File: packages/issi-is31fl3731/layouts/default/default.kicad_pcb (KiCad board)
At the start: 2 copper layers, 11 parts

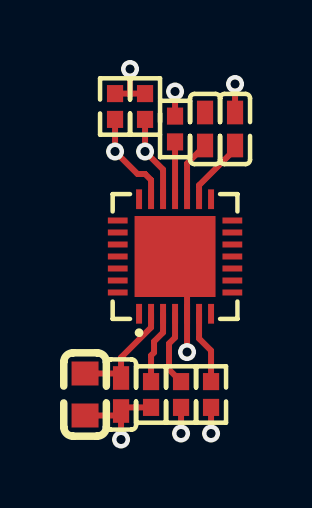
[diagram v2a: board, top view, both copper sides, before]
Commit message: Upgrade Packages: Narayans Half (#185)
* adi-ad5693r

* fix frozen

* prjc-teensy_4_1

* rp2040

* adi-adxl375: Add missing usage build target to ato.yaml

* adi-ds2482s-800: Update layout files after build

* adi-ltc4311: Update layout to fix frozen build

- Updated net names (BUS1/BUS2 → SDA/SCL, gnd → GND, hv → VCC)
- Fixed footprint properties and coordinates
- Package now passes frozen build and verification

* awinic-aw9523: Update layout to fix frozen build

- Updated net names (AD0/AD1 → address_bit_0/address_bit_1, hv → VCC, gnd → GND)
- Updated GPIO line names (-line-0 → gpios[8]-line, etc.)
- Fixed footprint properties and coordinates
- Package now passes frozen build and verification

* awinic-aw9523: Bump version to 0.1.1

- Version bump due to layout updates to fix frozen build

* adi-adbms6830: Fix package verify issues

- Add has_part_removed trait to components missing pickers (atopile_logo, SPDT, analog_DPDT)
- Add missing import for has_part_removed trait
- Add exclude_checks to usage build in ato.yaml
- Update README.md to match usage.ato content
- Bump version from 0.1.2 to 0.1.3

Package now passes ato package verify -s

* indicator-leds: Update layout and bump version

- Updated PCB layout coordinates to fix frozen build issues
- Bumped version from 0.1.5 to 0.1.6
- Package now passes ato package verify -s successfully

* Bump package versions for done packages

- adi-adxl345: 0.1.1 -> 0.1.2
- adi-adxl375: 0.1.0 -> 0.1.1
- adi-ds2482s-800: 0.1.0 -> 0.1.1
- adi-ltc4311: 0.1.0 -> 0.1.1
- adi-ltc4316: 0.1.0 -> 0.1.1
- ams-tsl2591: 0.1.0 -> 0.1.1

These packages were marked as 'Done' in package-todos.md but had version
warnings during package verification. Version bumps ensure they can be
published to the registry.

* invensense-mpu6050: Update layout files and bump version to 0.1.2

* Fix picker warnings by adding has_part_removed trait to MCU modules

- Added #pragma experiment("TRAITS") to enable traits feature
- Added import has_part_removed t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
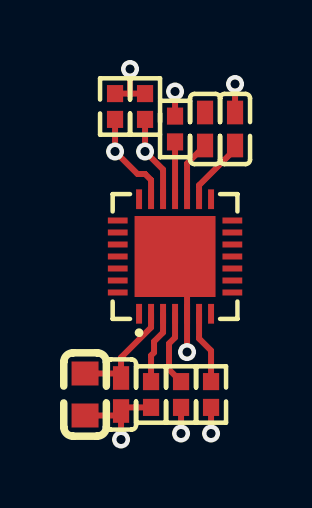
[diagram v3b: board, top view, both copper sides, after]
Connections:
- net gnd renamed GND

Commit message: fix some more packages
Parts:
- C1, C4, C5: value 100nF ±10% 16V X7R -> {8.99999998509884e-08..1.1000000014901162e-07}F
- C2: value 10µF ±20% 6.3V X5R -> {8.999999985098837e-06..1.1000000014901161e-05}F
- R1: value 20kΩ ±1% 62.5mW -> {20000.0±1.0%}Ω
- R2, R3, R6: value 10kΩ ±1% 62.5mW -> {10000.0±1.0%}Ω
- R4, R5: value 10kΩ ±1% 62.5mW -> {4700.0±1.0%}Ω
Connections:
- net CA1 renamed 21
- net CA2 renamed 22
- net CA3 renamed 23
- net CA4 renamed 24
- net CA5 renamed 25
- net CA6 renamed 26
- net CA7 renamed 27
- net CA8 renamed 28
- net CA9 renamed 1
- net CB1 renamed 7
- net CB2 renamed 8
- net CB3 renamed 9
- net CB4 renamed 10
- net CB5 renamed 11
- net CB6 renamed 12
- net CB7 renamed 13
- net CB8 renamed 14
- net CB9 renamed 15
- net GND renamed filter_capacitor-power-lv
- net IN renamed audio_input_capacitor-power-lv
- net VCC renamed hv

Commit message: fix issi-is31fl3731
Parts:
- C1, C4, C5: value {8.99999998509884e-08..1.1000000014901162e-07}F -> 1.0000000000000001e-07F
- C2: value {8.999999985098837e-06..1.1000000014901161e-05}F -> 9.999999999999999e-06F
- R1: value {20000.0±1.0%}Ω -> 20000.0Ω
- R2, R3, R6: value {10000.0±1.0%}Ω -> 10000.0Ω
- R4, R5: value {4700.0±1.0%}Ω -> 4700.0Ω
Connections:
- net C_FILT renamed filter_capacitor-power-hv
- net hv renamed decoupling_capacitor_small-power-hv
- net line renamed audio_input_capacitor-power-hv

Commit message: fix reference shim fix
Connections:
- net audio_input_capacitor-power-hv renamed hv
- net audio_input_capacitor-power-lv renamed lv
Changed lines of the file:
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@@
 	(net 23 "filter_capacitor-power-lv")
 	(net 24 "R_EXT")
-	(net 25 "audio_input_capacitor-power-lv")
+	(net 25 "lv")
 	(net 26 "INTB")
 	(net 27 "decoupling_capacitor_small-power-hv")
 	(net 28 "SDB")
-	(net 29 "audio_input_capacitor-power-hv")
+	(net 29 "hv")
 	(footprint "UNI_ROYAL_0402WGF1002TCE:R0402"
 		(layer "F.Cu")
@@
 			(size 0.5 0.54)
 			(layers "F.Cu" "F.Paste" "F.Mask")
-			(net 29 "audio_input_capacitor-power-hv")
+			(net 29 "hv")
 		)
 		(pad "2" smd rect
@@
 			(size 0.5 0.54)
 			(layers "F.Cu" "F.Paste" "F.Mask")
-			(net 25 "audio_input_capacitor-power-lv")
+			(net 25 "lv")
 		)
 		(embedded_fonts no)
@@
 			(size 0.2 0.66)
 			(layers "F.Cu" "F.Paste" "F.Mask")
-			(net 25 "audio_input_capacitor-power-lv")
+			(net 25 "lv")
 		)
 		(pad "18" smd rect

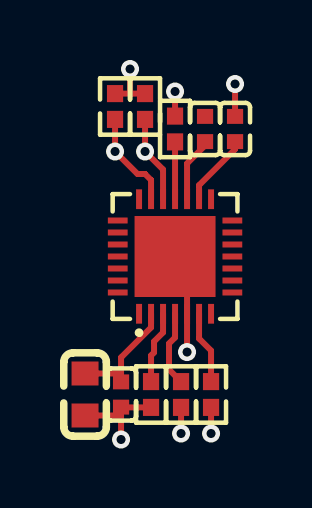
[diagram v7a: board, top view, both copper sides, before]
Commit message: remove all those other changes, just bosch baby
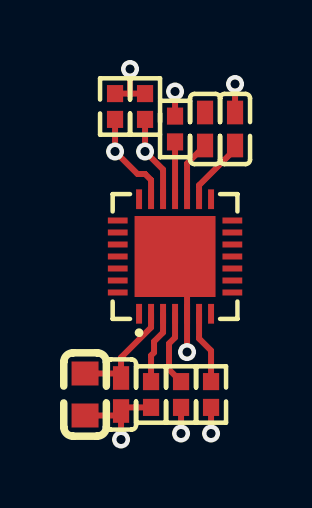
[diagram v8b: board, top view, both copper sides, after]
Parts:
- C1, C4, C5: value 1.0000000000000001e-07F -> 100nF ±10% 16V X7R
- C2: value 9.999999999999999e-06F -> 10µF ±20% 6.3V X5R
- R1: value 20000.0Ω -> 20kΩ ±1% 62.5mW
- R2, R3, R6: value 10000.0Ω -> 10kΩ ±1% 62.5mW
- R4, R5: value 4700.0Ω -> 10kΩ ±1% 62.5mW
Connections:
- net 1 renamed CA9
- net 10 renamed CB4
- net 11 renamed CB5
- net 12 renamed CB6
- net 13 renamed CB7
- net 14 renamed CB8
- net 15 renamed CB9
- net 21 renamed CA1
- net 22 renamed CA2
- net 23 renamed CA3
- net 24 renamed CA4
- net 25 renamed CA5
- net 26 renamed CA6
- net 27 renamed CA7
- net 28 renamed CA8
- net 7 renamed CB1
- net 8 renamed CB2
- net 9 renamed CB3
- net decoupling_capacitor_small-power-hv renamed VCC
- net filter_capacitor-power-hv renamed C_FILT
- net filter_capacitor-power-lv renamed GND
- net hv renamed line
- net lv renamed IN
